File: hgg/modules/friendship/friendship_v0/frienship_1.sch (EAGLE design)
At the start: 31 parts, among them IC5 741G66DBV, IC6 741G66DBV, IC7 741G66DBV, IC8 741G66DBV

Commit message: fixed a bug: shift enable must be defaulted to low
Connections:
- net 3V3: no longer IRQ_LATCHA.INH, PRSNT_LATCHA.INH
- net GND: now also IRQ_LATCHA.INH, PRSNT_LATCHA.INH
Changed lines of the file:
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@@
 <setting verticaltext="up"/>
 </settings>
-<grid distance="0.05" unitdist="inch" unit="inch" style="lines" multiple="1" display="no" altdistance="0.01" altunitdist="inch" altunit="inch"/>
+<grid distance="0.1" unitdist="inch" unit="inch" style="lines" multiple="1" display="no" altdistance="0.01" altunitdist="inch" altunit="inch"/>
 <layers>
 <layer number="1" name="Top" color="4" fill="1" visible="no" active="no"/>
@@
 <part name="R11" library="rcl" deviceset="R-EU_" device="R0603" value="120"/>
 <part name="R13" library="rcl" deviceset="R-EU_" device="R0603" value="120"/>
+<part name="GND19" library="supply1" deviceset="GND" device=""/>
+<part name="GND22" library="supply1" deviceset="GND" device=""/>
 </parts>
 <sheets>
@@
 <instance part="R11" gate="G$1" x="-71.12" y="241.3" rot="R270"/>
 <instance part="R13" gate="G$1" x="-77.47" y="241.3" rot="R270"/>
+<instance part="GND19" gate="1" x="-139.7" y="-30.48" rot="R90"/>
+<instance part="GND22" gate="1" x="-139.7" y="-73.66" rot="R90"/>
 </instances>
 <busses>
@@
 <pinref part="GND29" gate="1" pin="GND"/>
 </segment>
+<segment>
+<pinref part="PRSNT_LATCH" gate="A" pin="INH"/>
+<pinref part="GND19" gate="1" pin="GND"/>
+<wire x1="-142.24" y1="-30.48" x2="-144.78" y2="-30.48" width="0.1524" layer="91"/>
+</segment>
+<segment>
+<pinref part="IRQ_LATCH" gate="A" pin="INH"/>
+<pinref part="GND22" gate="1" pin="GND"/>
+<wire x1="-142.24" y1="-73.66" x2="-144.78" y2="-73.66" width="0.1524" layer="91"/>
+</segment>
 </net>
 <net name="RX+" class="0">
@@
 </segment>
 <segment>
-<pinref part="PRSNT_LATCH" gate="A" pin="INH"/>
-<wire x1="-144.78" y1="-30.48" x2="-109.22" y2="-30.48" width="0.1524" layer="91"/>
-</segment>
-<segment>
-<pinref part="IRQ_LATCH" gate="A" pin="INH"/>
-<wire x1="-144.78" y1="-73.66" x2="-109.22" y2="-73.66" width="0.1524" layer="91"/>
-</segment>
-<segment>

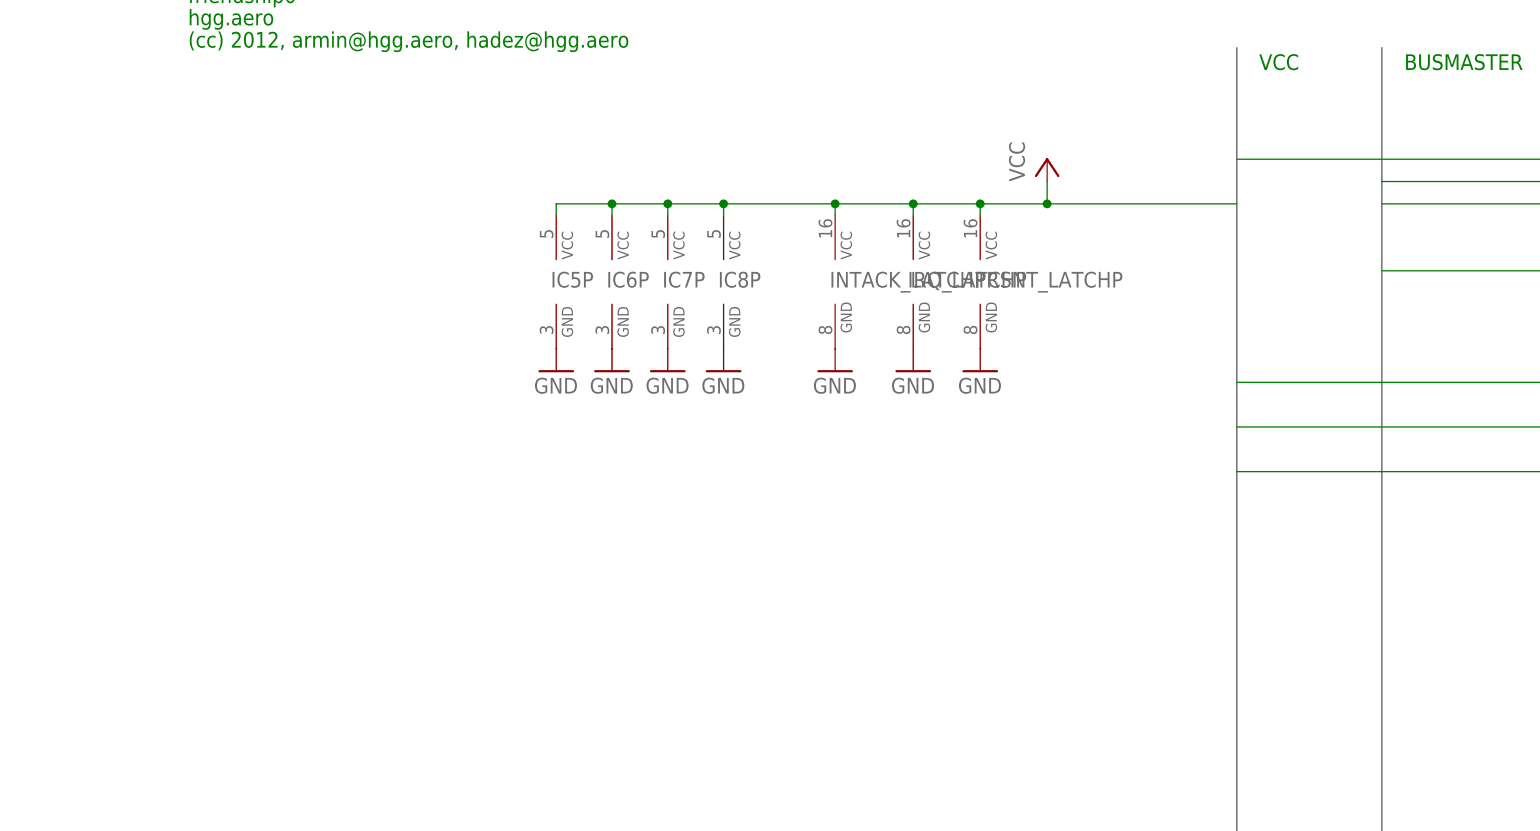
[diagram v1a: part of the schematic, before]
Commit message: added pullups to IRQ lines
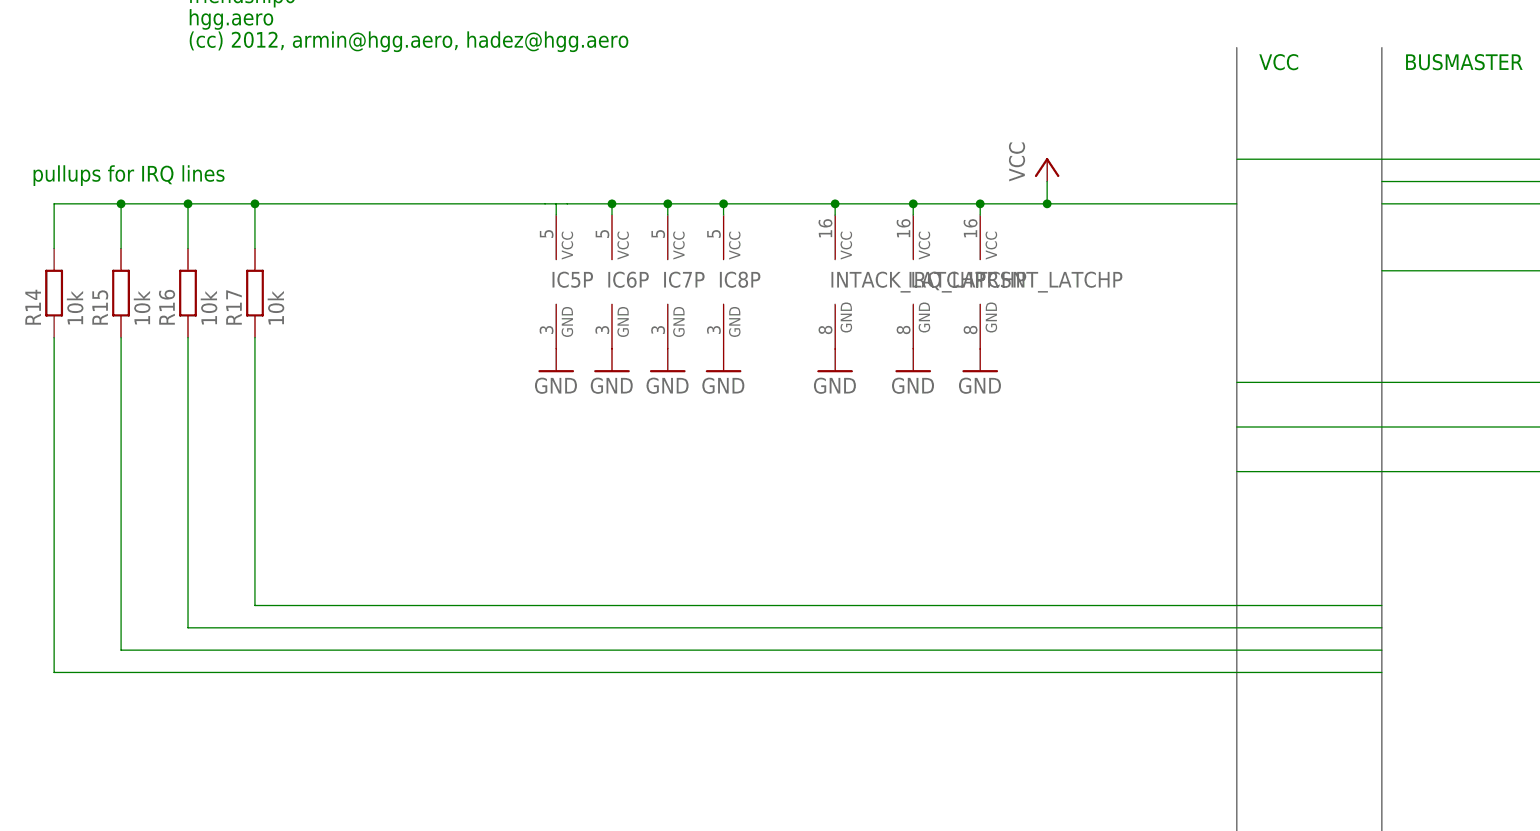
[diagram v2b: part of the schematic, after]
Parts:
- added R14, R15, R16, R17: 10k, rcl:R-EU_R0603
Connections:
- net 3V3: now also R14.2, R15.2, R16.2, R17.2
- net IRQ0: now also R17.1
- net IRQ1: now also R16.1
- net IRQ2: now also R15.1
- net IRQ3: now also R14.1
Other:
- note added: "pullups for IRQ lines"
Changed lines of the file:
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@@
 <setting verticaltext="up"/>
 </settings>
-<grid distance="0.1" unitdist="inch" unit="inch" style="lines" multiple="1" display="no" altdistance="0.01" altunitdist="inch" altunit="inch"/>
+<grid distance="0.05" unitdist="inch" unit="inch" style="lines" multiple="1" display="no" altdistance="0.01" altunitdist="inch" altunit="inch"/>
 <layers>
 <layer number="1" name="Top" color="4" fill="1" visible="no" active="no"/>
@@
 <part name="GND19" library="supply1" deviceset="GND" device=""/>
 <part name="GND22" library="supply1" deviceset="GND" device=""/>
+<part name="R14" library="rcl" deviceset="R-EU_" device="R0603" value="10k"/>
+<part name="R15" library="rcl" deviceset="R-EU_" device="R0603" value="10k"/>
+<part name="R16" library="rcl" deviceset="R-EU_" device="R0603" value="10k"/>
+<part name="R17" library="rcl" deviceset="R-EU_" device="R0603" value="10k"/>
 </parts>
 <sheets>
@@
 <text x="-228.6" y="218.44" size="1.778" layer="91">This work by hackerspace global grid is licensed under a Creative Commons Attribution-NonCommercial-ShareAlike 3.0 Unported License.</text>
 <text x="-228.6" y="210.82" size="1.778" layer="91">(cc) 2012, armin@hgg.aero, hadez@hgg.aero</text>
+<text x="-246.38" y="195.58" size="1.778" layer="91">pullups for IRQ lines</text>
 </plain>
 <instances>
@@
 <instance part="GND19" gate="1" x="-139.7" y="-30.48" rot="R90"/>
 <instance part="GND22" gate="1" x="-139.7" y="-73.66" rot="R90"/>
+<instance part="R14" gate="G$1" x="-243.84" y="182.88" rot="R90"/>
+<instance part="R15" gate="G$1" x="-236.22" y="182.88" rot="R90"/>
+<instance part="R16" gate="G$1" x="-228.6" y="182.88" rot="R90"/>
+<instance part="R17" gate="G$1" x="-220.98" y="182.88" rot="R90"/>
 </instances>
 <busses>
@@
 <pinref part="IRQ_LATCH" gate="A" pin="D"/>
 </segment>
+<segment>
+<wire x1="-92.71" y1="147.32" x2="-220.98" y2="147.32" width="0.1524" layer="91"/>
+<wire x1="-220.98" y1="147.32" x2="-220.98" y2="177.8" width="0.1524" layer="91"/>
+<pinref part="R17" gate="G$1" pin="1"/>
+</segment>
 </net>
 <net name="/CS0" class="0">
@@
 <pinref part="IRQ_LATCH" gate="A" pin="C"/>
 </segment>
+<segment>
+<pinref part="R16" gate="G$1" pin="1"/>
+<wire x1="-92.71" y1="144.78" x2="-228.6" y2="144.78" width="0.1524" layer="91"/>
+<wire x1="-228.6" y1="144.78" x2="-228.6" y2="177.8" width="0.1524" layer="91"/>
+</segment>
 </net>
 <net name="/CS1" class="0">
@@
 <pinref part="IRQ_LATCH" gate="A" pin="B"/>
 </segment>
+<segment>
+<pinref part="R15" gate="G$1" pin="1"/>
+<wire x1="-92.71" y1="142.24" x2="-236.22" y2="142.24" width="0.1524" layer="91"/>
+<wire x1="-236.22" y1="142.24" x2="-236.22" y2="177.8" width="0.1524" layer="91"/>
+</segment>
 </net>
 <net name="/CS2" class="0">
@@
 <pinref part="IRQ_LATCH" gate="A" pin="A"/>
 <wire x1="-129.54" y1="-99.06" x2="-144.78" y2="-99.06" width="0.1524" layer="91"/>
+</segment>
+<segment>
+<pinref part="R14" gate="G$1" pin="1"/>
+<wire x1="-92.71" y1="139.7" x2="-243.84" y2="139.7" width="0.1524" layer="91"/>
+<wire x1="-243.84" y1="139.7" x2="-243.84" y2="177.8" width="0.1524" layer="91"/>
 </segment>
 </net>
@@
 <junction x="-173.99" y="193.04"/>
 <pinref part="IC5" gate="P" pin="VCC"/>
-<wire x1="-180.34" y1="193.04" x2="-186.69" y2="193.04" width="0.1524" layer="91"/>
+<wire x1="-180.34" y1="193.04" x2="-185.42" y2="193.04" width="0.1524" layer="91"/>
 <wire x1="-186.69" y1="193.04" x2="-186.69" y2="191.77" width="0.1524" layer="91"/>
 <junction x="-180.34" y="193.04"/>
-</segment>
-</net>
+<pinref part="R14" gate="G$1" pin="2"/>
+<wire x1="-243.84" y1="187.96" x2="-243.84" y2="193.04" width="0.1524" layer="91"/>
+<wire x1="-243.84" y1="193.04" x2="-236.22" y2="193.04" width="0.1524" layer="91"/>
+<pinref part="R15" gate="G$1" pin="2"/>
+<wire x1="-236.22" y1="193.04" x2="-228.6" y2="193.04" width="0.1524" layer="91"/>
+<wire x1="-228.6" y1="193.04" x2="-220.98" y2="193.04" width="0.1524" layer="91"/>
+<wire x1="-220.98" y1="193.04" x2="-187.96" y2="193.04" width="0.1524" layer="91"/>
+<wire x1="-187.96" y1="193.04" x2="-186.69" y2="193.04" width="0.1524" layer="91"/>
+<wire x1="-236.22" y1="187.96" x2="-236.22" y2="193.04" width="0.1524" layer="91"/>
+<junction x="-236.22" y="193.04"/>
+<pinref part="R16" gate="G$1" pin="2"/>
+<wire x1="-228.6" y1="187.96" x2="-228.6" y2="193.04" width="0.1524" layer="91"/>
+<junction x="-228.6" y="193.04"/>
+<pinref part="R17" gate="G$1" pin="2"/>
+<wire x1="-220.98" y1="187.96" x2="-220.98" y2="193.04" width="0.1524" layer="91"/>
+<junction x="-220.98" y="193.04"/>
+<wire x1="-186.69" y1="193.04" x2="-185.42" y2="193.04" width="0.1524" layer="91"/>
+</segment>
+</net>
